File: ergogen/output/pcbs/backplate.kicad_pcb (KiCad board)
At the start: 2 copper layers, 130.1 x 94.7 mm, 5 parts

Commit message: feat: outline improvements
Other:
- board size 130.1 x 94.7 mm -> 134.9 x 109.8 mm
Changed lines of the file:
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@@
     )
   )
-  (gr_line (start 110.50826649856596 109.92527651860325) (end 91.48622889852672 39.83343914341975) (layer Edge.Cuts) (stroke (width 0.15) (type default)))
-(gr_line (start 91.9687610950968 39.202482330781216) (end 127.8150135 39.201513513148655) (layer Edge.Cuts) (stroke (width 0.15) (type default)))
+  (gr_line (start 91.2502786953727 111.93679999635788) (end 91.31455549192064 39.702041598866344) (layer Edge.Cuts) (stroke (width 0.15) (type default)))
+(gr_line (start 91.81454179192065 39.202486498870485) (end 127.8150135 39.20151351314865) (layer Edge.Cuts) (stroke (width 0.15) (type default)))
 (gr_line (start 128.315 38.701513513148655) (end 128.315 35.3275) (layer Edge.Cuts) (stroke (width 0.15) (type default)))
 (gr_line (start 128.815 34.8275) (end 146.315 34.8275) (layer Edge.Cuts) (stroke (width 0.15) (type default)))
@@
 (gr_line (start 183.34287840000002 37.12312159204324) (end 200.8424827703032 37.12737825256575) (layer Edge.Cuts) (stroke (width 0.15) (type default)))
 (gr_line (start 201.34236077036712 37.628016802540515) (end 201.31863938512134 56.201861450012075) (layer Edge.Cuts) (stroke (width 0.15) (type default)))
-(gr_line (start 220.93800000000002 112.3635) (end 219.65752596395185 126.98539423067496) (layer Edge.Cuts) (stroke (width 0.15) (type default)))
-(gr_line (start 219.08114720800037 127.43560839237159) (end 120.6993432 111.83961029999999) (layer Edge.Cuts) (stroke (width 0.15) (type default)))
-(gr_line (start 118.6165232 111.50943079999999) (end 110.91252714391037 110.28815311369672) (layer Edge.Cuts) (stroke (width 0.15) (type default)))
+(gr_line (start 221.6070711821377 104.9663415844974) (end 226.0923281969262 115.6359149762103) (layer Edge.Cuts) (stroke (width 0.15) (type default)))
+(gr_line (start 226.0654764006069 116.07782689603465) (end 211.09156059668345 142.27125340028437) (layer Edge.Cuts) (stroke (width 0.15) (type default)))
+(gr_line (start 210.44136417514045 142.47398553796899) (end 176.60167485384602 126.25365946744344) (layer Edge.Cuts) (stroke (width 0.15) (type default)))
+(gr_line (start 176.4280428580794 126.20634746780448) (end 161.62301991140092 124.94372737349019) (layer Edge.Cuts) (stroke (width 0.15) (type default)))
+(gr_line (start 161.4782637171782 124.95248967103738) (end 144.8505883399894 128.42692930209176) (layer Edge.Cuts) (stroke (width 0.15) (type default)))
+(gr_line (start 144.74831955000005 128.4375) (end 124.6650889942857 128.4375) (layer Edge.Cuts) (stroke (width 0.15) (type default)))
+(gr_line (start 124.44649265438869 128.38718392921672) (end 91.53168215547566 112.38692882557845) (layer Edge.Cuts) (stroke (width 0.15) (type default)))
 (gr_line (start 201.81863898518517 56.7025) (end 221.068 56.7025) (layer Edge.Cuts) (stroke (width 0.15) (type default)))
-(gr_line (start 221.568 57.2025) (end 221.568 111.8635) (layer Edge.Cuts) (stroke (width 0.15) (type default)))
-(gr_line (start 221.068 112.3635) (end 220.93800000000002 112.3635) (layer Edge.Cuts) (stroke (width 0.15) (type default)))
-(gr_arc (start 91.9687610950968 39.20248233078121) (mid 91.5716065950968 39.39874303078121) (end 91.48622889509679 39.83343913078121) (layer Edge.Cuts) (stroke (width 0.15) (type default)))
+(gr_line (start 221.568 57.2025) (end 221.568 104.77257712698844) (layer Edge.Cuts) (stroke (width 0.15) (type default)))
+(gr_arc (start 91.81454179192065 39.202486498863436) (mid 91.46115449192064 39.348780598863435) (end 91.31455549192064 39.70204159886344) (layer Edge.Cuts) (stroke (width 0.15) (type default)))
 (gr_arc (start 127.81501349999999 39.201513513148655) (mid 128.1685582 39.05506211314866) (end 128.315 38.701513513148655) (layer Edge.Cuts) (stroke (width 0.15) (type default)))
 (gr_arc (start 128.815 34.8275) (mid 128.4614466 34.9739466) (end 128.315 35.3275) (layer Edge.Cuts) (stroke (width 0.15) (type default)))
@@
 (gr_arc (start 201.31863938518518 56.20186150001397) (mid 201.46485988518518 56.55582760001397) (end 201.81863908518517 56.70250000001397) (layer Edge.Cuts) (stroke (width 0.15) (type default)))
 (gr_arc (start 221.568 57.2025) (mid 221.42155340000002 56.8489466) (end 221.068 56.7025) (layer Edge.Cuts) (stroke (width 0.15) (type default)))
-(gr_arc (start 221.068 112.3635) (mid 221.42155340000002 112.2170534) (end 221.568 111.8635) (layer Edge.Cuts) (stroke (width 0.15) (type default)))
-(gr_arc (start 219.08114715922605 127.43560838463978) (mid 219.46721955922604 127.33581428463978) (end 219.65752595922604 126.98539428463978) (layer Edge.Cuts) (stroke (width 0.15) (type default)))
-(gr_arc (start 110.50826649513606 109.92527650596477) (mid 110.65681719513606 110.16640490596477) (end 110.91252709513606 110.28815320596476) (layer Edge.Cuts) (stroke (width 0.15) (type default)))
+(gr_arc (start 221.568 104.77257712698844) (mid 221.57786510000003 104.87140932698844) (end 221.6070712 104.96634152698844) (layer Edge.Cuts) (stroke (width 0.15) (type default)))
+(gr_arc (start 226.0654763790639 116.07782693371927) (mid 226.1304788790639 115.86000493371927) (end 226.0923281790639 115.63591503371926) (layer Edge.Cuts) (stroke (width 0.15) (type default)))
+(gr_arc (start 210.44136417514042 142.47398553796899) (mid 210.80631727514043 142.50044073796897) (end 211.09156057514042 142.27125343796897) (layer Edge.Cuts) (stroke (width 0.15) (type default)))
+(gr_arc (start 176.60167485384602 126.25365946744346) (mid 176.51700495384603 126.22212736744345) (end 176.42804285384602 126.20634746744345) (layer Edge.Cuts) (stroke (width 0.15) (type default)))
+(gr_arc (start 161.62301990716756 124.94372737312915) (mid 161.55032240716756 124.94283237312915) (end 161.47826370716757 124.95248957312914) (layer Edge.Cuts) (stroke (width 0.15) (type default)))
+(gr_arc (start 144.74831955000005 128.4375) (mid 144.79972635000004 128.4348503) (end 144.85058835000004 128.4269294) (layer Edge.Cuts) (stroke (width 0.15) (type default)))
+(gr_arc (start 124.4464926942857 128.3871839) (mid 124.5529327942857 128.4247586) (end 124.6650889942857 128.4375) (layer Edge.Cuts) (stroke (width 0.15) (type default)))
+(gr_arc (start 91.25027869537269 111.93679999636173) (mid 91.32631019537268 112.20229379636173) (end 91.53168219537268 112.38692879636173) (layer Edge.Cuts) (stroke (width 0.15) (type default)))
 (gr_circle (center 109.25 73.75) (end 110.35 73.75) (layer Edge.Cuts) (stroke (width 0.15) (type default)) (fill none))
 (gr_circle (center 109.25 91.25) (end 110.35 91.25) (layer Edge.Cuts) (stroke (width 0.15) (type default)) (fill none))
 (gr_circle (center 183.218 70.4235) (end 184.31799999999998 70.4235) (layer Edge.Cuts) (stroke (width 0.15) (type default)) (fill none))
-(gr_arc (start 120.6993432 111.83961029999999) (mid 119.87922710000001 110.2785665) (end 118.6165232 111.50943079999999) (layer Edge.Cuts) (stroke (width 0.15) (type default)))
+(gr_circle (center 119.70700000000001 111.365) (end 120.807 111.365) (layer Edge.Cuts) (stroke (width 0.15) (type default)) (fill none))
 (gr_circle (center 191.871694 109.48666770000001) (end 192.97169399999999 109.48666770000001) (layer Edge.Cuts) (stroke (width 0.15) (type default)) (fill none))
 )

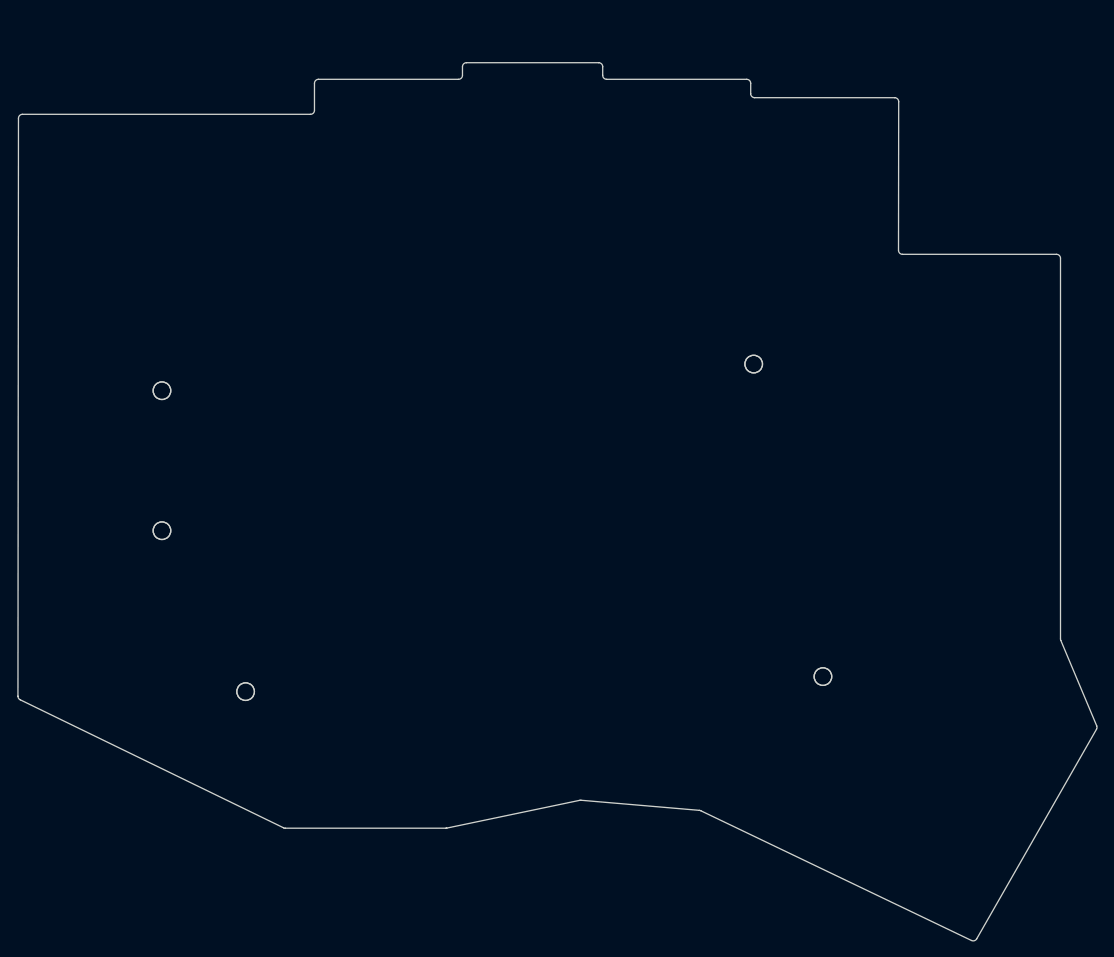
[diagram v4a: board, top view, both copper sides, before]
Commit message: feat: PCB holes alignment
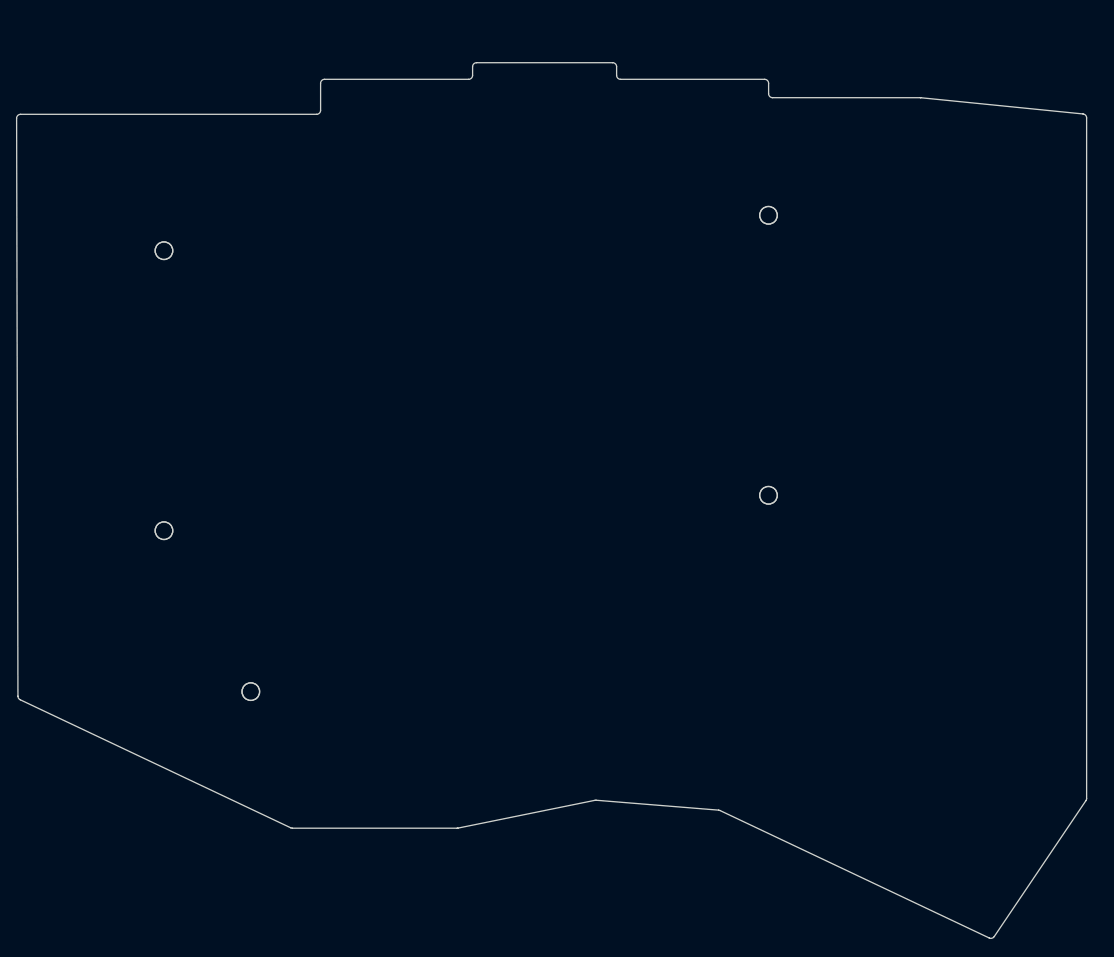
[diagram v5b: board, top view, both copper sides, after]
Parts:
- moved MH5 71.5 mm to (120.4, 111.4), turned to 0 degrees
- moved MH4 69.8 mm to (185.1, 86.8)
- moved MH3 18.7 mm to (185.1, 51.8)
- moved MH1 17.5 mm to (109.5, 56.2)
- moved MH2 0.25 mm to (109.5, 91.2)
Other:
- board size 134.9 x 109.8 mm -> 133.8 x 109.5 mm
